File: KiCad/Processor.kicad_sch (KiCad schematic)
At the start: 9 parts, among them U1 Intel_P24T

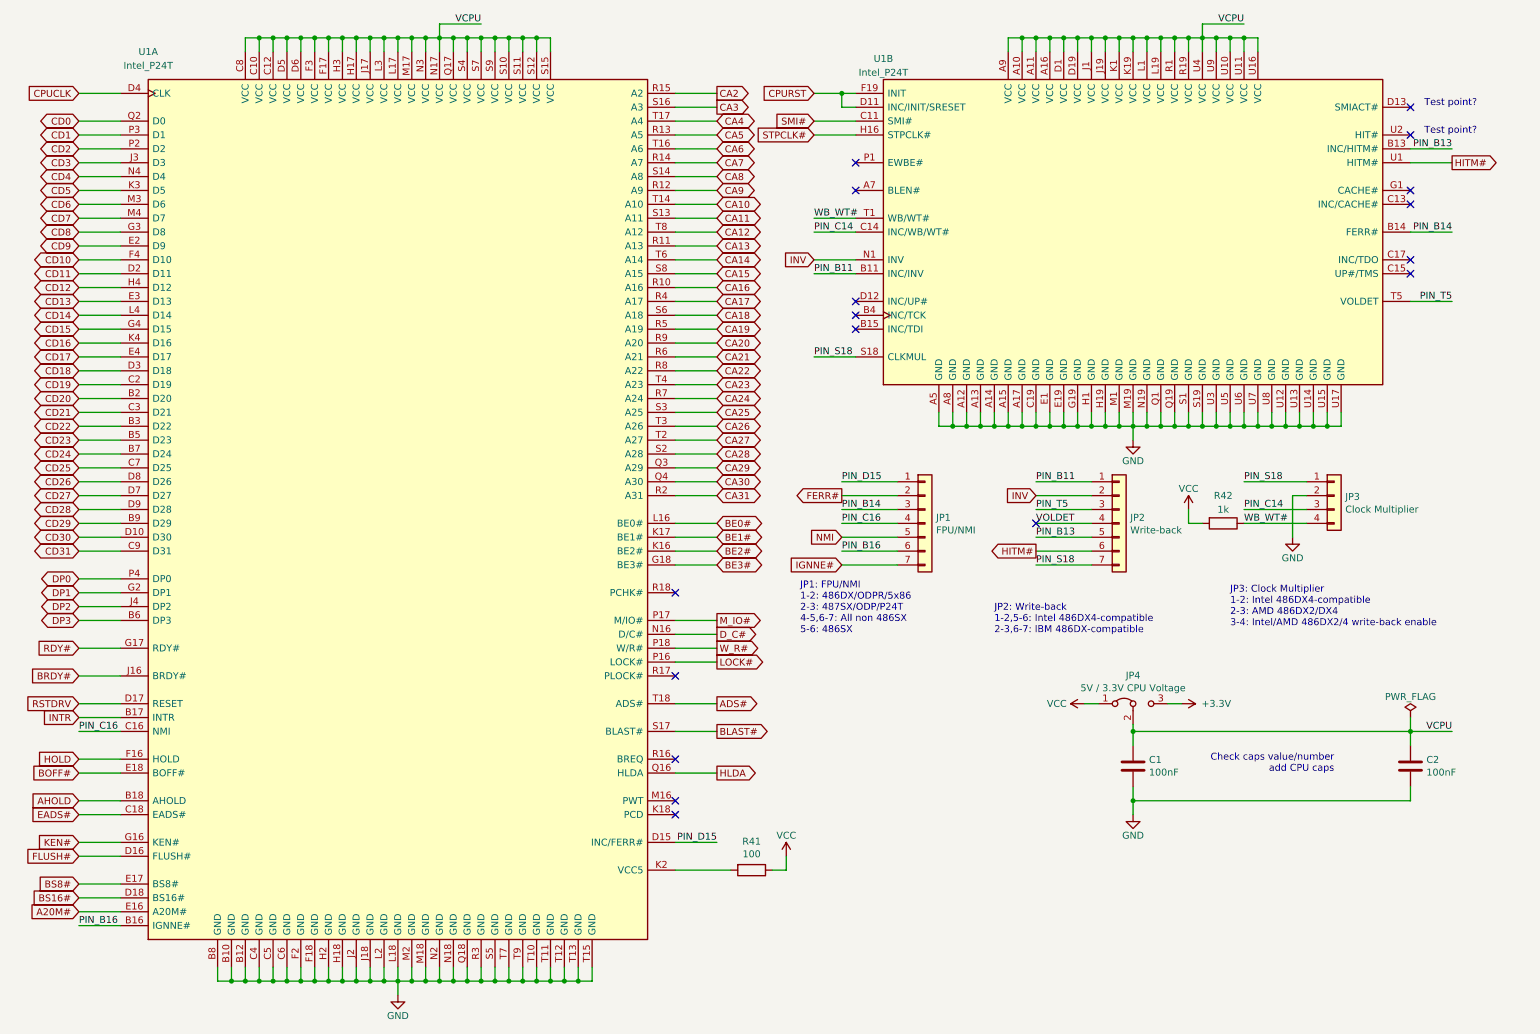
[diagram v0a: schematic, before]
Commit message: Version 0.3: Update DRAM schematic, pull-ups/pull-downs, CPU configuration jumpers
Signed-off-by: Sergey Kiselev <skiselev@gmail.com>
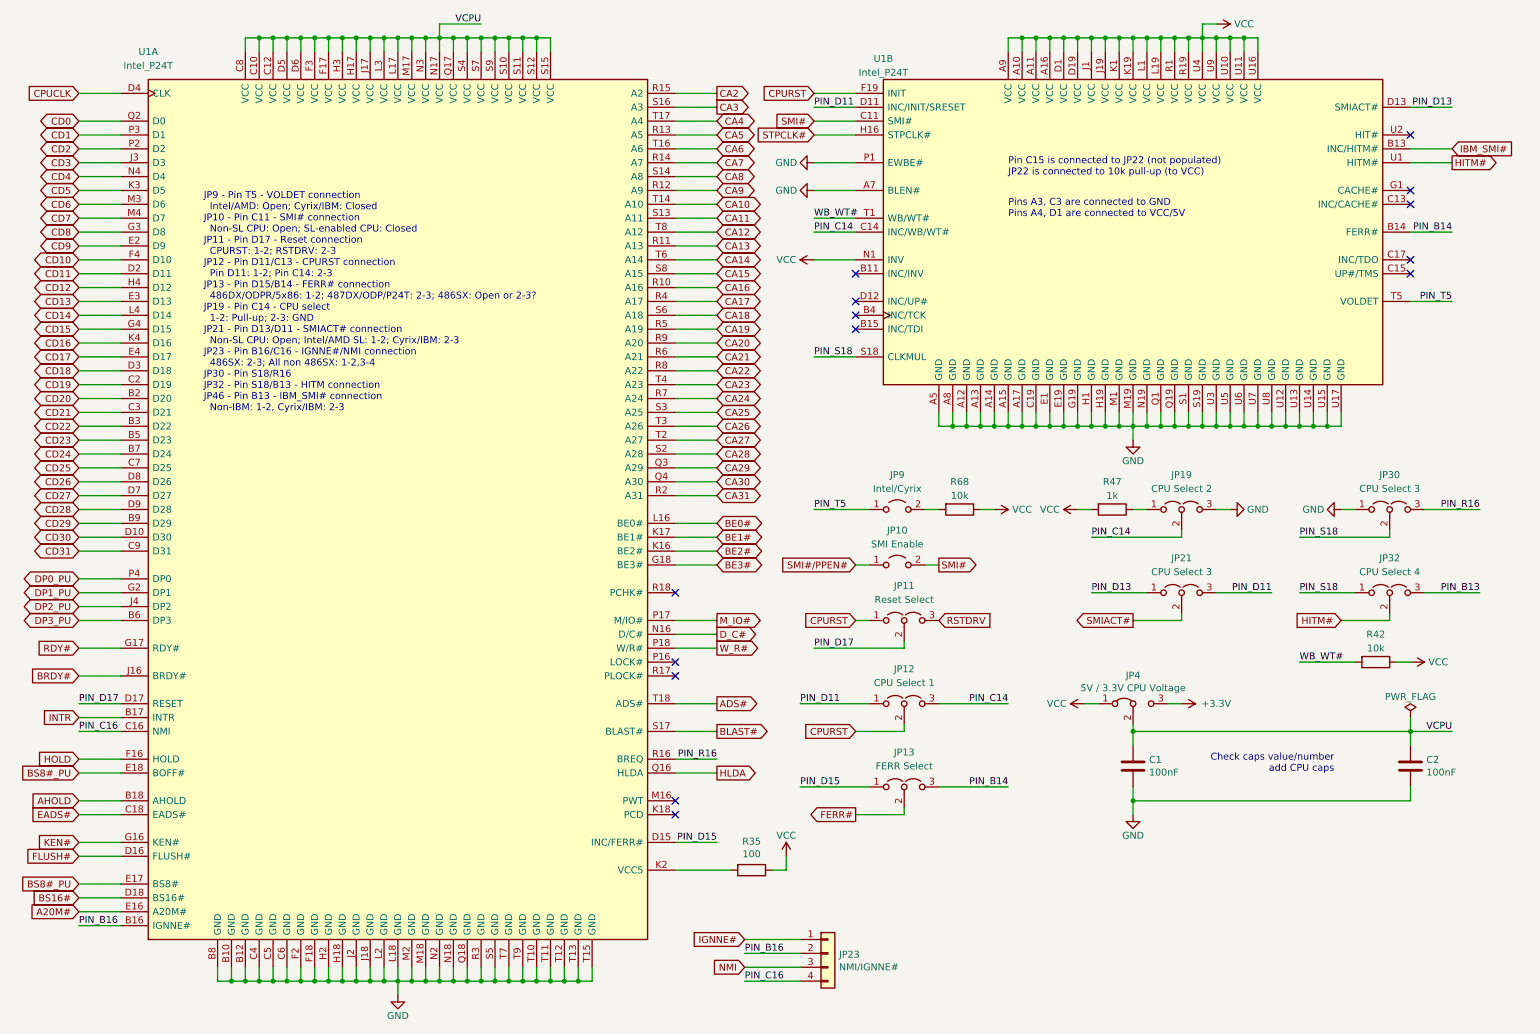
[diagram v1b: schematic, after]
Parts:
- removed JP1: FPU/NMI, symbol Connector_Generic:Conn_01x07
- removed JP2: Write-back, symbol Connector_Generic:Conn_01x07
- removed JP3: Clock Multiplier, symbol Connector_Generic:Conn_01x04
- added JP10: SMI Enable, symbol Jumper:Jumper_2_Open
- added JP11: Reset Select, symbol Jumper:Jumper_3_Open
- added JP12: CPU Select 1, symbol Jumper:Jumper_3_Open
- added JP13: FERR Select, symbol Jumper:Jumper_3_Open
- added JP19: CPU Select 2, symbol Jumper:Jumper_3_Open
- added JP21, JP30: CPU Select 3, symbol Jumper:Jumper_3_Open
- added JP23: NMI/IGNNE#, symbol Connector_Generic:Conn_01x04
- added JP32: CPU Select 4, symbol Jumper:Jumper_3_Open
- added JP9: Intel/Cyrix, symbol Jumper:Jumper_2_Open
- added R47: 1k, symbol Device:R
- added R68: 10k, symbol Device:R
- R42: value 1k -> 10k
- renumbered R41 to R35
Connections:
- net BS8# is gone; now on net BS8#_PU: U1.E17 (BS8#)
- net INV is gone; now on net VCC: U1.N1 (INV)
- net CPURST: now also JP11.1 (A), JP12.2 (C); no longer U1.D11 (INC/INIT/SRESET)
- net FERR#: now also JP13.2 (C)
- net GND: now also U1.A7 (BLEN#), U1.P1 (EWBE#), JP19.3 (B), JP30.1 (A)
- net HITM#: now also JP32.2 (C)
- net IGNNE#: now also JP23.1 (Pin_1)
- net NMI: now also JP23.3 (Pin_3)
- net PIN_B13: now also JP32.3 (B); no longer U1.B13 (INC/HITM#)
- net PIN_B14: now also JP13.3 (B)
- net PIN_B16: now also JP23.2 (Pin_2)
- net PIN_C14: now also JP12.3 (B), JP19.2 (C)
- net PIN_C16: now also JP23.4 (Pin_4)
- net PIN_D15: now also JP13.1 (A)
- net PIN_S18: now also JP30.2 (C), JP32.1 (A)
- net PIN_T5: now also JP9.1 (A)
- net RSTDRV: now also JP11.3 (B); no longer U1.D17 (RESET)
- net SMI#: now also JP10.2 (B)
- net VCC: now also R42.1, U1.A10 (VCC), U1.A11 (VCC), U1.A16 (VCC), U1.A9 (VCC), U1.D1 (VCC), U1.D19 (VCC), U1.J1 (VCC), U1.J19 (VCC), U1.K1 (VCC), U1.K19 (VCC), U1.L1 (VCC), U1.L19 (VCC), U1.R1 (VCC), U1.R19 (VCC), U1.U10 (VCC), U1.U11 (VCC), U1.U16 (VCC), U1.U4 (VCC), U1.U9 (VCC), R47.2, R68.1; no longer R42.2
- net VCPU: no longer U1.A10 (VCC), U1.A11 (VCC), U1.A16 (VCC), U1.A9 (VCC), U1.D1 (VCC), U1.D19 (VCC), U1.J1 (VCC), U1.J19 (VCC), U1.K1 (VCC), U1.K19 (VCC), U1.L1 (VCC), U1.L19 (VCC), U1.R1 (VCC), U1.R19 (VCC), U1.U10 (VCC), U1.U11 (VCC), U1.U16 (VCC), U1.U4 (VCC), U1.U9 (VCC)
- net WB_WT#: now also R42.2; no longer R42.1
- net PIN_R16: now reaches U1.R16 (BREQ)
- net PIN_R16: now also JP30.3 (B)
- net PIN_D13: now reaches U1.D13 (SMIACT#)
- net PIN_D13: now also JP21.1 (A)
- net BOFF# renamed BS8#_PU
- net DP0 renamed DP0_PU
- net DP1 renamed DP1_PU
- net DP2 renamed DP2_PU
- net DP3 renamed DP3_PU
- net LOCK#: no longer names the net of U1.P16 (LOCK#)
- net PIN_B11: no longer names the net of U1.B11 (INC/INV)
- new net: JP9.2 (B), R68.2
- new net: JP19.1 (A), R47.1
- new net IBM_SMI#: U1.B13 (INC/HITM#)
- new net PIN_D11: JP12.1 (A), JP21.3 (B), U1.D11 (INC/INIT/SRESET)
- new net PIN_D17: JP11.2 (C), U1.D17 (RESET)
- new net SMI#/PPEN#: JP10.1 (A)
- new net SMIACT#: JP21.2 (C)
- no-connect marks 17 -> 14
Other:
- note added: "JP9 - Pin T5 - VOLDET connection Intel/AMD: Open; Cyrix/IBM: Closed JP10 - Pin C11 - SMI# connection Non-SL CPU: Open; SL-enabled CPU: Closed JP11 - Pin D17 - Reset connection CPURST: 1-2; RSTDRV: 2-3 JP12 - Pin D11/C13 - CPURST connection Pin D11: 1-2; Pin C14: 2-3 JP13 - Pin D15/B14 - FERR# connection 486DX/ODPR/5x86: 1-2; 487DX/ODP/P24T: 2-3; 486SX: Open or 2-3? JP19 - Pin C14 - CPU select 1-2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"
- note added: "Pin C15 is connected to JP22 (not populated) JP22 is connected to 10k pull-up (to VCC)"
- note added: "Pins A3, C3 are connected to GND Pins A4, D1 are connected to VCC/5V"
- note removed: "JP1: FPU/NMI 1-2: 486DX/ODPR/5x86 2-3: 487SX/ODP/P24T 4-5,6-7: All non 486SX 5-6: 486SX"
- note removed: "JP2: Write-back 1-2,5-6: Intel 486DX4-compatible 2-3,6-7: IBM 486DX-compatible"
- note removed: "JP3: Clock Multiplier 1-2: Intel 486DX4-compatible 2-3: AMD 486DX2/DX4 3-4: Intel/AMD 486DX2/4 write-back enable"
- note removed: "Test point?"

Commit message: Version 0.4: Update chipset connection
Signed-off-by: Sergey Kiselev <skiselev@gmail.com>
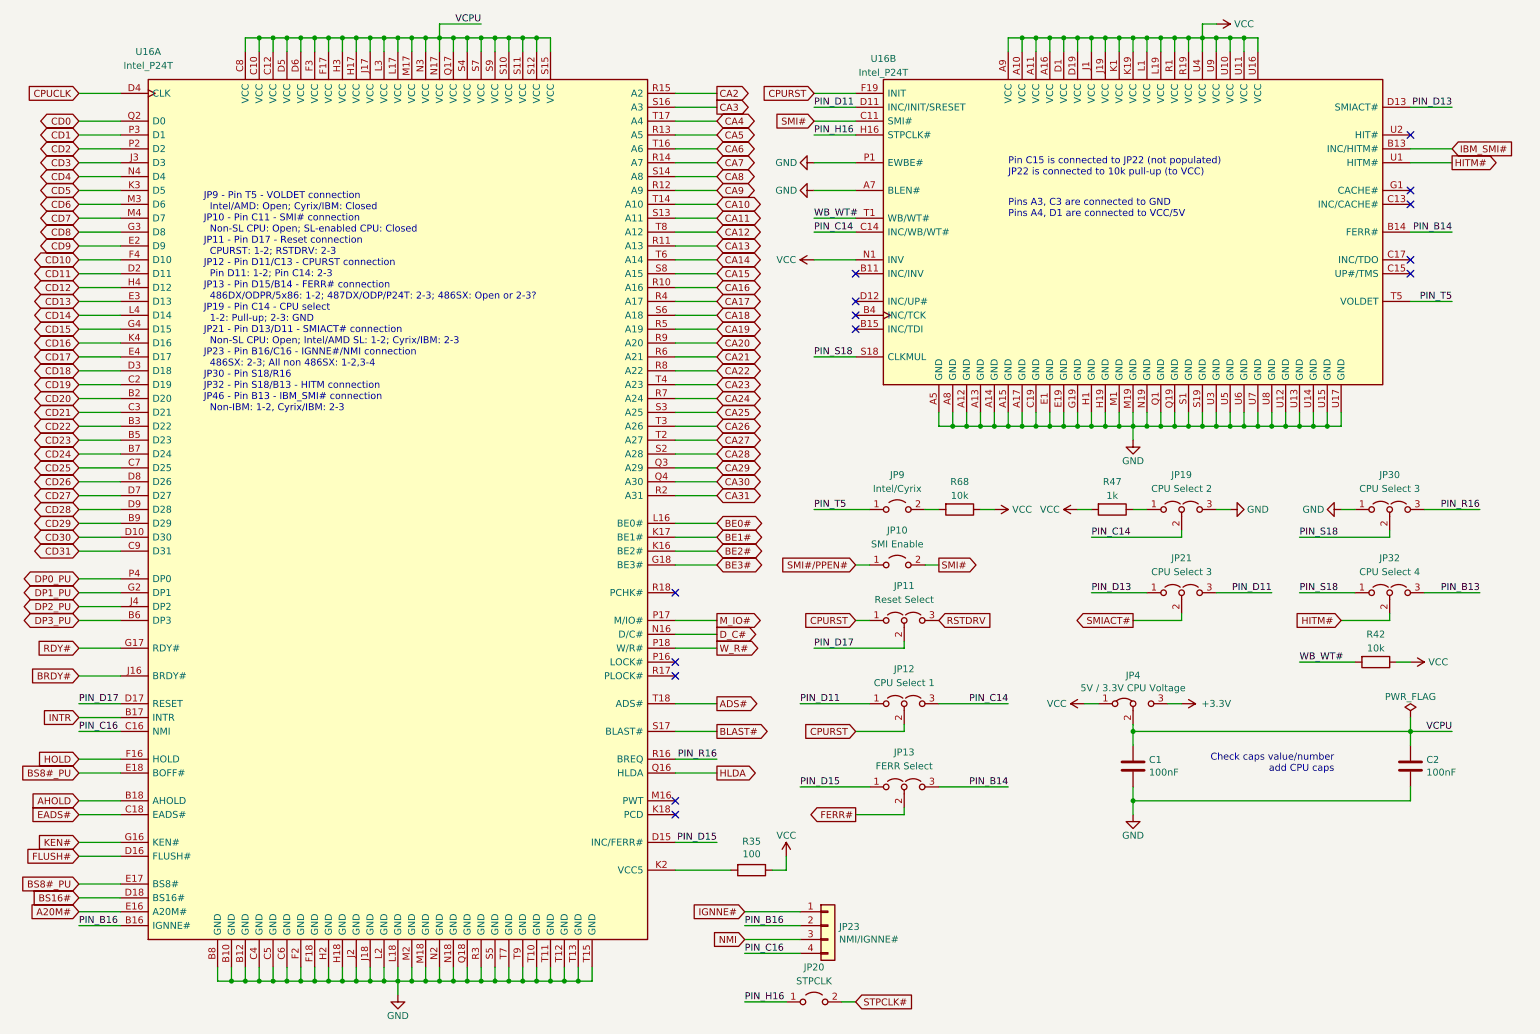
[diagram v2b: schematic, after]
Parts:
- added JP20: STPCLK, My_Components:Conn_Pin_Header_2x1_2.54mm, symbol Jumper:Jumper_2_Open
- C1, C2: footprint (none) -> Capacitor_SMD:C_0603_1608Metric_Pad1.08x0.95mm_HandSolder
- JP10, JP9: footprint (none) -> My_Components:Conn_Pin_Header_2x1_2.54mm
- JP11, JP12, JP13, JP19, JP21, JP30, JP32, JP4: footprint (none) -> My_Components:Conn_Pin_Header_3x1_2.54mm
- JP23: footprint (none) -> My_Components:Conn_Pin_Header_4x1_2.54mm
- R35, R42, R47, R68: footprint (none) -> Resistor_SMD:R_0612_1632Metric_Pad1.18x3.40mm_HandSolder
- renumbered U1 to U16
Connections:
- net STPCLK#: now also JP20.2 (B); no longer U16.H16 (STPCLK#)
- new net PIN_H16: JP20.1 (A), U16.H16 (STPCLK#)
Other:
- moved on the sheet: JP23
